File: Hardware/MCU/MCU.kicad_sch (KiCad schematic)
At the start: 3 parts, among them J1 Conn_ARM_JTAG_SWD_10, U1 ESP32-S3-WROOM-1

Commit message: MCU schema bijgewerkt
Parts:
- removed J1: Conn_ARM_JTAG_SWD_10, Connector_PinHeader_1.27mm:PinHeader_2x05_P1.27mm_Horizontal, symbol Connector:Conn_ARM_JTAG_SWD_10
- added C2, C3: C, symbol Device:C
- added J1: USB_C_Receptacle_USB2.0_14P, symbol Connector:USB_C_Receptacle_USB2.0_14P
- added J3: Conn_01x05_Pin_i2c1, symbol Connector:Conn_01x05_Pin
- added J4: Conn_01x05_Pin_i2s, symbol Connector:Conn_01x05_Pin
- added J5: Conn_01x07_Pin_spi0, symbol Connector:Conn_01x07_Pin
- added J6: Conn_01x07_Pin_spi1, symbol Connector:Conn_01x07_Pin
- added J7: Conn_01x07_Pin_spi2, symbol Connector:Conn_01x07_Pin
- added J8: Conn_02x13_Counter_Clockwise_gpio, symbol Connector_Generic:Conn_02x13_Counter_Clockwise
- added J9: Conn_01x06_Pin_i2c0, symbol Connector:Conn_01x06_Pin
- added R1, R2, R5: 5k1, symbol Device:R
- added R10, R11, R12, R13: 4k7, symbol Device:R
- added R3, R4: 0, symbol Device:R
- added R6, R9: 470, symbol Device:R
- added R7, R8: 10k, symbol Device:R
- added SW1, SW2: SW_Push, symbol Switch:SW_Push
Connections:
- net +3.3V: now also J3.2 (Pin_2), J4.2 (Pin_2), J5.2 (Pin_2), J6.2 (Pin_2), J7.2 (Pin_2), J8.2 (Pin_2), J8.25 (Pin_25), J9.2 (Pin_2), R10.2, R11.1, R12.2, R13.1, R5.1, R7.1, R8.1
- net GND: now also C2.1, C3.1, J1.A1 (GND), J1.A12 (GND), J1.B1 (GND), J1.B12 (GND), J1.S1 (SHIELD), J3.1 (Pin_1), J4.1 (Pin_1), J5.1 (Pin_1), J6.1 (Pin_1), J7.1 (Pin_1), J8.1 (Pin_1), J8.26 (Pin_26), J9.1 (Pin_1), R1.1, R2.1, R6.2, R9.2
- net io17: now reaches U1.10 (IO17)
- net io17: now also J8.9 (Pin_9)
- net io18: now reaches U1.11 (IO18)
- net io18: now also J8.10 (Pin_10)
- net ss2: now reaches U1.12 (IO8)
- net ss2: now also J7.6 (Pin_6)
- net at U1.13 (USB_D-): now also C2.2, R4.1
- net at U1.14 (USB_D+): now also C3.2, R3.1
- net sda0: now reaches U1.15 (IO3)
- net sda0: now also J9.3 (Pin_3), R13.2
- net io46: now reaches U1.16 (IO46)
- net io46: now also J8.17 (Pin_17)
- net ss1: now reaches U1.17 (IO9)
- net ss1: now also J6.6 (Pin_6)
- net ss0: now reaches U1.18 (IO10)
- net ss0: now also J5.6 (Pin_6)
- net mosi: now reaches U1.19 (IO11)
- net mosi: now also J5.5 (Pin_5), J6.5 (Pin_5), J7.5 (Pin_5)
- net sck: now reaches U1.20 (IO12)
- net sck: now also J5.4 (Pin_4), J6.4 (Pin_4), J7.4 (Pin_4)
- net miso: now reaches U1.21 (IO13)
- net miso: now also J5.3 (Pin_3), J6.3 (Pin_3), J7.3 (Pin_3)
- net io14: now reaches U1.22 (IO14)
- net io14: now also J8.6 (Pin_6)
- net io21: now reaches U1.23 (IO21)
- net io21: now also J8.24 (Pin_24)
- net io47: now reaches U1.24 (IO47)
- net io47: now also J8.16 (Pin_16)
- net io48: now reaches U1.25 (IO48)
- net io48: now also J8.15 (Pin_15)
- net io45: now reaches U1.26 (IO45)
- net io45: now also J8.18 (Pin_18)
- net boot0: now reaches U1.27 (IO0)
- net boot0: now also R7.2, SW1.1
- net io35: now reaches U1.28 (IO35)
- net io35: now also J8.23 (Pin_23)
- net io36: now reaches U1.29 (IO36)
- net io36: now also J8.22 (Pin_22)
- net reset: now reaches U1.3 (EN)
- net reset: now also R8.2, SW2.1
- net io37: now reaches U1.30 (IO37)
- net io37: now also J8.21 (Pin_21)
- net io38: now reaches U1.31 (IO38)
- net io38: now also J8.20 (Pin_20)
- net rxd0: now reaches U1.36 (RXD0)
- net rxd0: now also J8.12 (Pin_12)
- net txd0: now reaches U1.37 (TXD0)
- net txd0: now also J8.11 (Pin_11)
- net scl0: now reaches U1.38 (IO2)
- net scl0: now also J9.4 (Pin_4), R12.1
- net io1: now reaches U1.39 (IO1)
- net io1: now also J8.3 (Pin_3)
- net scl1: now reaches U1.4 (IO4)
- net scl1: now also J3.4 (Pin_4), R10.1
- net sda1: now reaches U1.5 (IO5)
- net sda1: now also J3.3 (Pin_3), R11.2
- net io6: now reaches U1.6 (IO6)
- net io6: now also J8.4 (Pin_4)
- net io7: now reaches U1.7 (IO7)
- net io7: now also J8.5 (Pin_5)
- net io15: now reaches U1.8 (IO15)
- net io15: now also J8.7 (Pin_7)
- net io16: now reaches U1.9 (IO16)
- net io16: now also J8.8 (Pin_8)
- net MTCK renamed io39
- net io39: now also J8.19 (Pin_19)
- net MTDI renamed i2s ws
- net i2s ws: now also J4.4 (Pin_4)
- net MTDO renamed i2s sck
- net i2s sck: now also J4.3 (Pin_3)
- net MTMS renamed i2s sd
- net i2s sd: now also J4.5 (Pin_5)
- new net: J1.A6 (D+), J1.B6 (D+), R3.2, R5.2
- new net: J1.A5 (CC1), R2.2
- new net: J1.A7 (D-), J1.B7 (D-), R4.2
- new net: J1.B5 (CC2), R1.2
- new net: R9.1, SW2.2
- new net: R6.1, SW1.2
- new net +5Vin: J3.5 (Pin_5), J5.7 (Pin_7), J6.7 (Pin_7), J7.7 (Pin_7), J8.13 (Pin_13), J8.14 (Pin_14), J9.6 (Pin_6)
- new net +5Vout: J1.A4 (VBUS), J1.A9 (VBUS), J1.B4 (VBUS), J1.B9 (VBUS), J9.5 (Pin_5)
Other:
- moved on the sheet: C1, U1

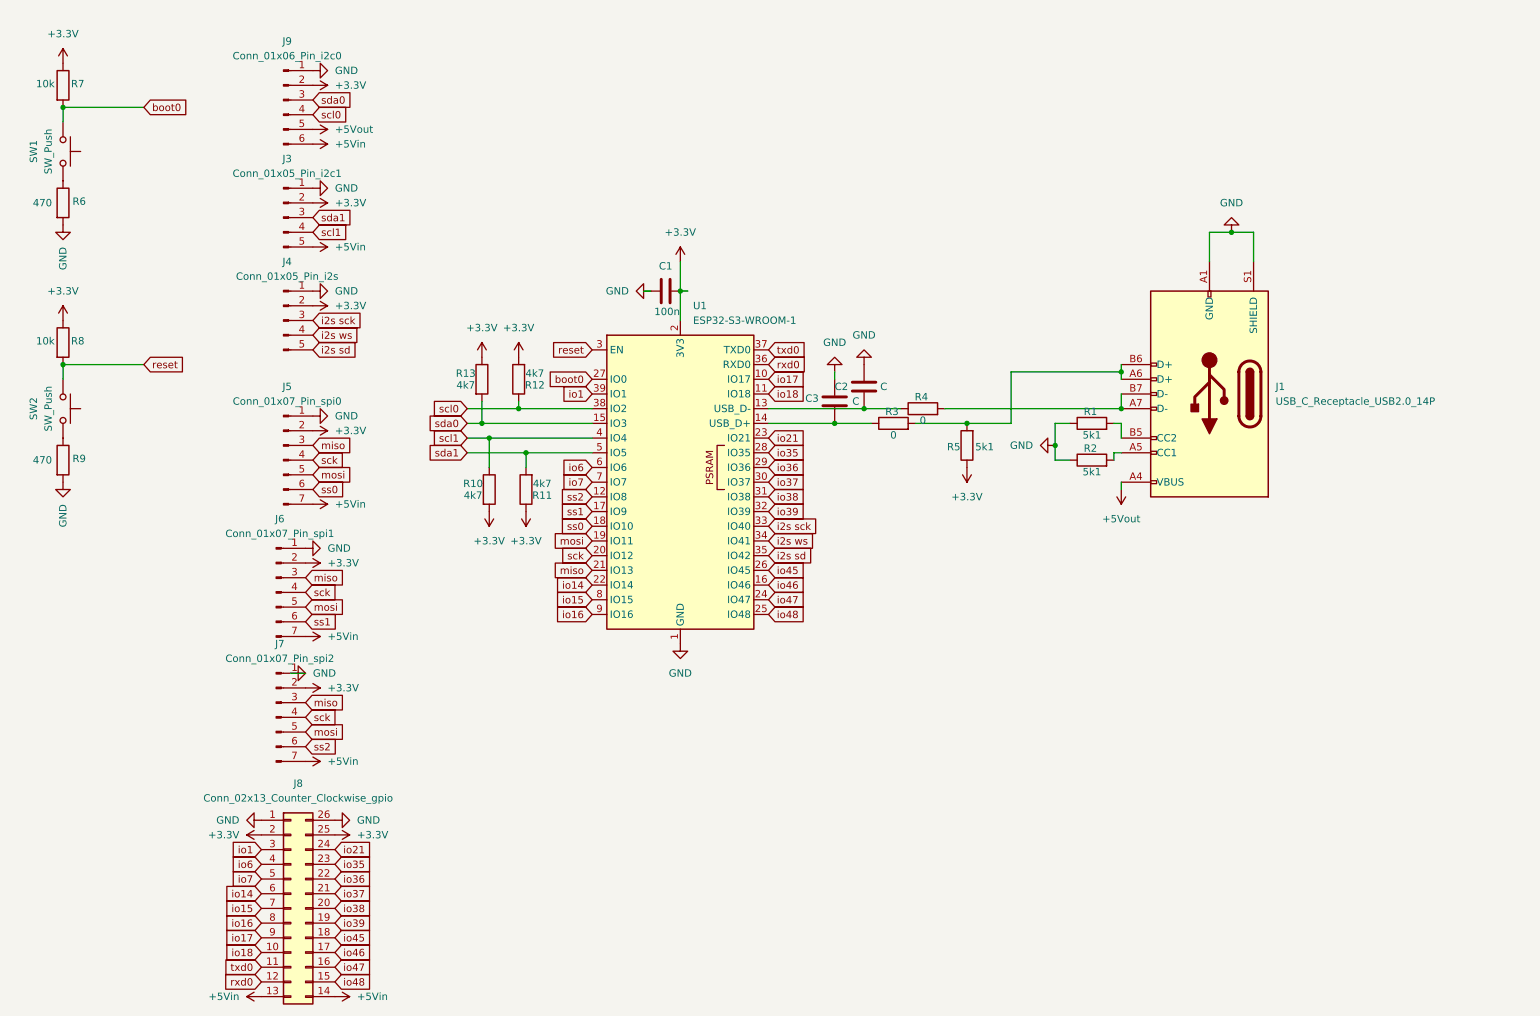
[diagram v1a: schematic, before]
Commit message: mcu design updated met layout en traces
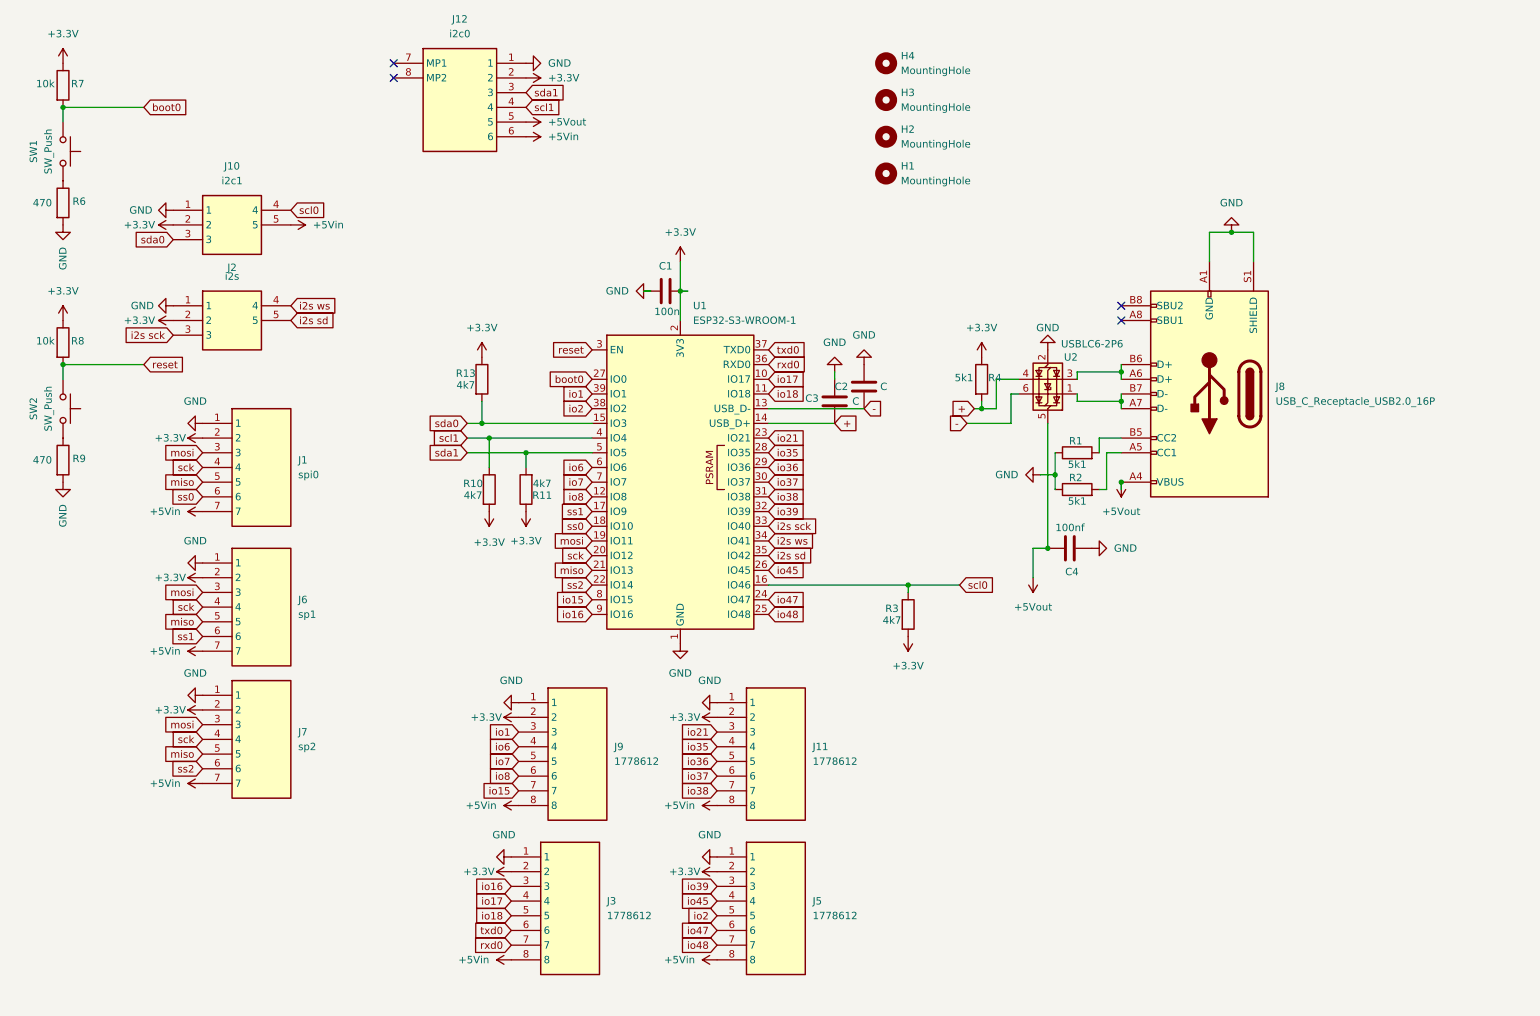
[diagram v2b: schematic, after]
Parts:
- removed J1: USB_C_Receptacle_USB2.0_14P, symbol Connector:USB_C_Receptacle_USB2.0_14P
- removed J3: Conn_01x05_Pin_i2c1, symbol Connector:Conn_01x05_Pin
- removed J4: Conn_01x05_Pin_i2s, symbol Connector:Conn_01x05_Pin
- removed J5: Conn_01x07_Pin_spi0, symbol Connector:Conn_01x07_Pin
- removed J6: Conn_01x07_Pin_spi1, symbol Connector:Conn_01x07_Pin
- removed J7: Conn_01x07_Pin_spi2, symbol Connector:Conn_01x07_Pin
- removed J8: Conn_02x13_Counter_Clockwise_gpio, symbol Connector_Generic:Conn_02x13_Counter_Clockwise
- removed J9: Conn_01x06_Pin_i2c0, symbol Connector:Conn_01x06_Pin
- removed R12: 4k7, symbol Device:R
- removed R5: 5k1, symbol Device:R
- added C4: 100nf, Capacitor_SMD:C_1206_3216Metric_Pad1.33x1.80mm_HandSolder, symbol Device:C
- added H1, H2, H3, H4: MountingHole, MountingHole:MountingHole_3.2mm_M3, symbol Mechanical:MountingHole
- added J1: spi0, 1778609, symbol Connector_pt_phoenix:1778609
- added J10: i2c1, Connector_pt_phoenix:1814948, symbol Connector_pt_phoenix:1814948
- added J11, J3, J5, J9: 1778612, 1778612, symbol Connector_pt_phoenix:1778612
- added J12: i2c0, Connector_pt_phoenix:1814951, symbol Connector_pt_phoenix:1814951
- added J2: i2s, Connector_pt_phoenix:1814948, symbol Connector_pt_phoenix:1814948
- added J6: sp1, 1778609, symbol Connector_pt_phoenix:1778609
- added J7: sp2, 1778609, symbol Connector_pt_phoenix:1778609
- added J8: USB_C_Receptacle_USB2.0_16P, Connector_USB:USB_C_Receptacle_G-Switch_GT-USB-7010ASV, symbol Connector:USB_C_Receptacle_USB2.0_16P
- added U2: USBLC6-2P6, Package_TO_SOT_SMD:SOT-666, symbol Power_Protection:USBLC6-2P6
- C1, C2, C3, SW1, SW2: footprint (none) -> Capacitor_SMD:C_1206_3216Metric_Pad1.33x1.80mm_HandSolder
- R1, R10, R11, R13, R2, R6, R7, R8, R9: footprint (none) -> Resistor_SMD:R_1206_3216Metric_Pad1.30x1.75mm_HandSolder
- R3: value 0 -> 4k7; footprint (none) -> Resistor_SMD:R_1206_3216Metric_Pad1.30x1.75mm_HandSolder
- R4: value 0 -> 5k1; footprint (none) -> Resistor_SMD:R_1206_3216Metric_Pad1.30x1.75mm_HandSolder
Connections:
- net io14 is gone; now on net ss2: U1.22 (IO14)
- net io46 is gone; now on net scl0: U1.16 (IO46)
- net +3.3V: now also R3.2, R4.1, J1.2, J10.2, J11.2, J12.2, J2.2, J3.2, J5.2, J6.2, J7.2, J9.2
- net +5Vin: now also J1.7, J10.5, J11.8, J12.6, J3.8, J5.8, J6.7, J7.7, J9.8
- net +5Vout: now also C4.1, J12.5, J8.A4 (VBUS), J8.A9 (VBUS), J8.B4 (VBUS), J8.B9 (VBUS), U2.5 (VBUS)
- net GND: now also C4.2, J1.1, J10.1, J11.1, J12.1, J2.1, J3.1, J5.1, J6.1, J7.1, J8.A1 (GND), J8.A12 (GND), J8.B1 (GND), J8.B12 (GND), J8.S1 (SHIELD), J9.1, U2.2 (GND)
- net i2s sck: now also J2.3
- net i2s sd: now also J2.5
- net i2s ws: now also J2.4
- net io1: now also J9.3
- net io15: now also J9.7
- net io16: now also J3.3
- net io17: now also J3.4
- net io18: now also J3.5
- net io21: now also J11.3
- net io35: now also J11.4
- net io36: now also J11.5
- net io37: now also J11.6
- net io38: now also J11.7
- net io39: now also J5.3
- net io45: now also J5.4
- net io47: now also J5.6
- net io48: now also J5.7
- net io6: now also J9.4
- net io7: now also J9.5
- net miso: now also J1.5, J6.5, J7.5
- net mosi: now also J1.3, J6.3, J7.3
- net rxd0: now also J3.7
- net sck: now also J1.4, J6.4, J7.4
- net scl0: now also R3.1, J10.4; no longer U1.38 (IO2)
- net scl1: now also J12.4
- net sda0: now also J10.3
- net sda1: now also J12.3
- net ss0: now also J1.6
- net ss1: now also J6.6
- net ss2: now also J7.6; no longer U1.12 (IO8)
- net txd0: now also J3.6
- net at R2.2: now also J8.A5 (CC1)
- net -: now reaches C2.2, U1.13 (USB_D-)
- net -: now also U2.6 (I/O1); no longer R4.1
- net +: now reaches C3.2, U1.14 (USB_D+)
- net +: now also R4.2, U2.4 (I/O2); no longer R3.1
- net at R1.2: now also J8.B5 (CC2)
- new net: J8.A7 (D-), J8.B7 (D-), U2.1 (I/O1)
- new net: J8.A6 (D+), J8.B6 (D+), U2.3 (I/O2)
- new net io2: J5.5, U1.38 (IO2)
- new net io8: J9.6, U1.12 (IO8)
- no-connect marks 0 -> 4
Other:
- moved on the sheet: R1, R2

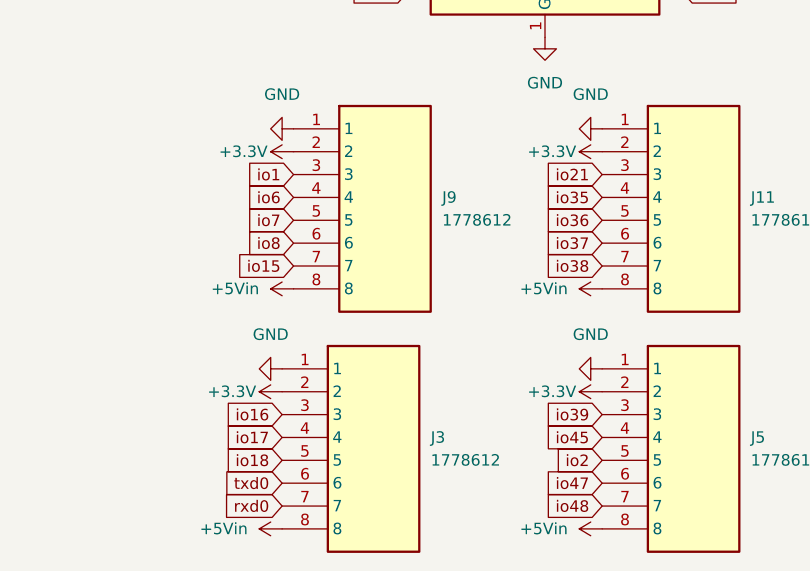
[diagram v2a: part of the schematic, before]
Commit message: updated traces en layout
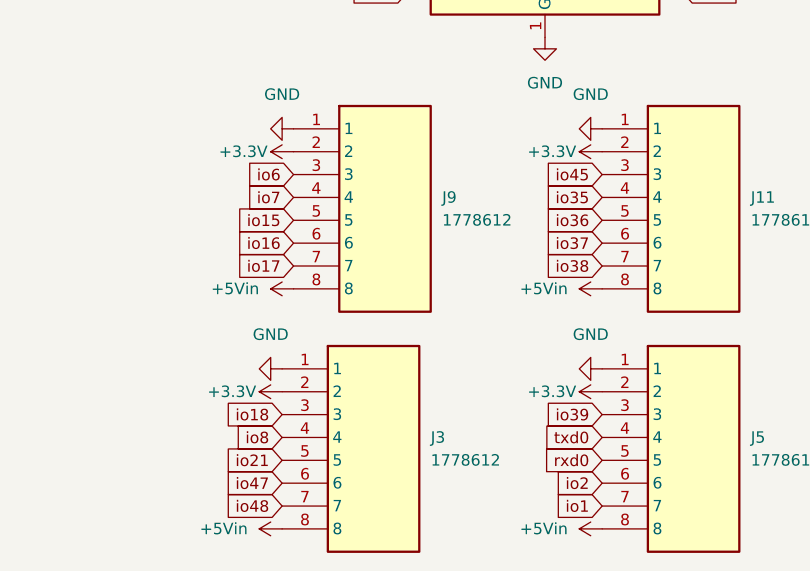
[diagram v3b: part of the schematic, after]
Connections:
- net io1: now also J5.7; no longer J9.3
- net io15: now also J9.5; no longer J9.7
- net io16: now also J9.6; no longer J3.3
- net io17: now also J9.7; no longer J3.4
- net io18: now also J3.3; no longer J3.5
- net io2: now also J5.6; no longer J5.5
- net io21: now also J3.5; no longer J11.3
- net io45: now also J11.3; no longer J5.4
- net io47: now also J3.6; no longer J5.6
- net io48: now also J3.7; no longer J5.7
- net io6: now also J9.3; no longer J9.4
- net io7: now also J9.4; no longer J9.5
- net io8: now also J3.4; no longer J9.6
- net rxd0: now also J5.5; no longer J3.7
- net txd0: now also J5.4; no longer J3.6
